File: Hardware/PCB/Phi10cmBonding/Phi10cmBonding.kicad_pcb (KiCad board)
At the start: 4 copper layers, 38.1 x 38.1 mm, 2 parts

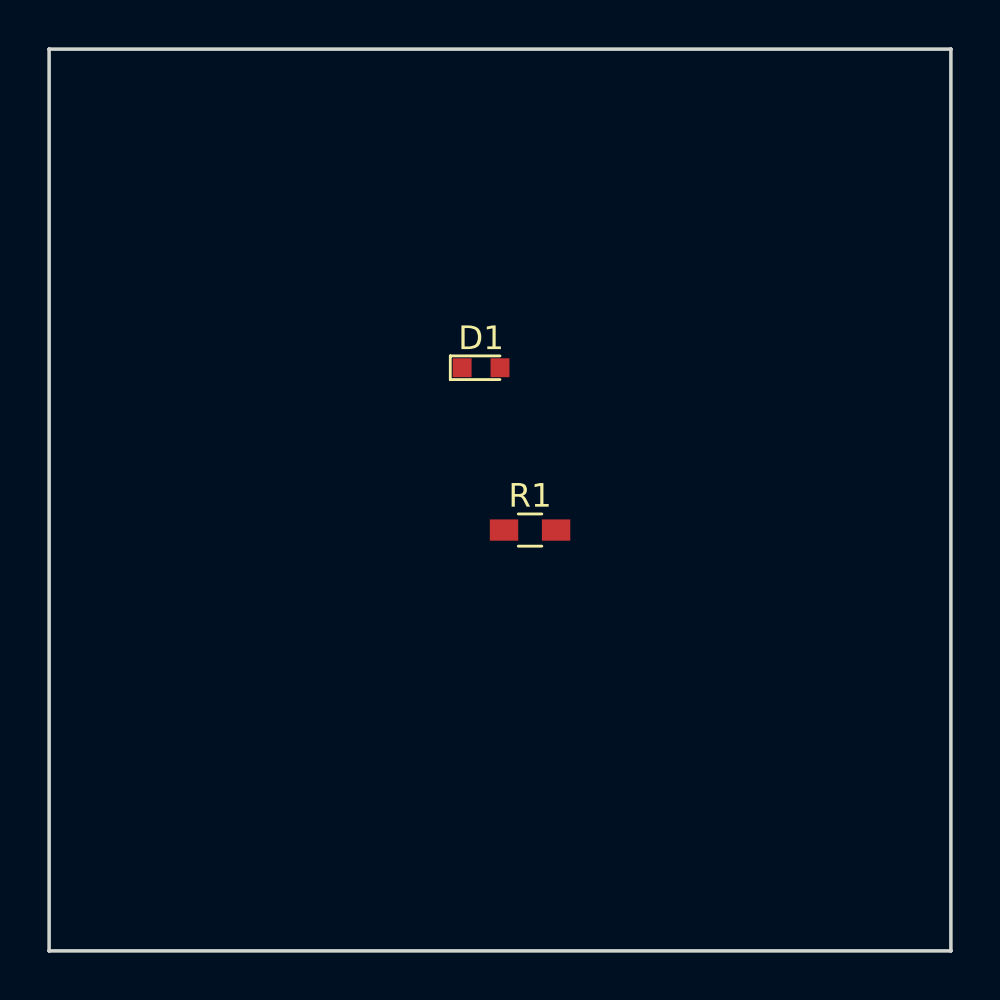
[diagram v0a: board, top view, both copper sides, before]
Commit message: First example of correct net handling and zone filling
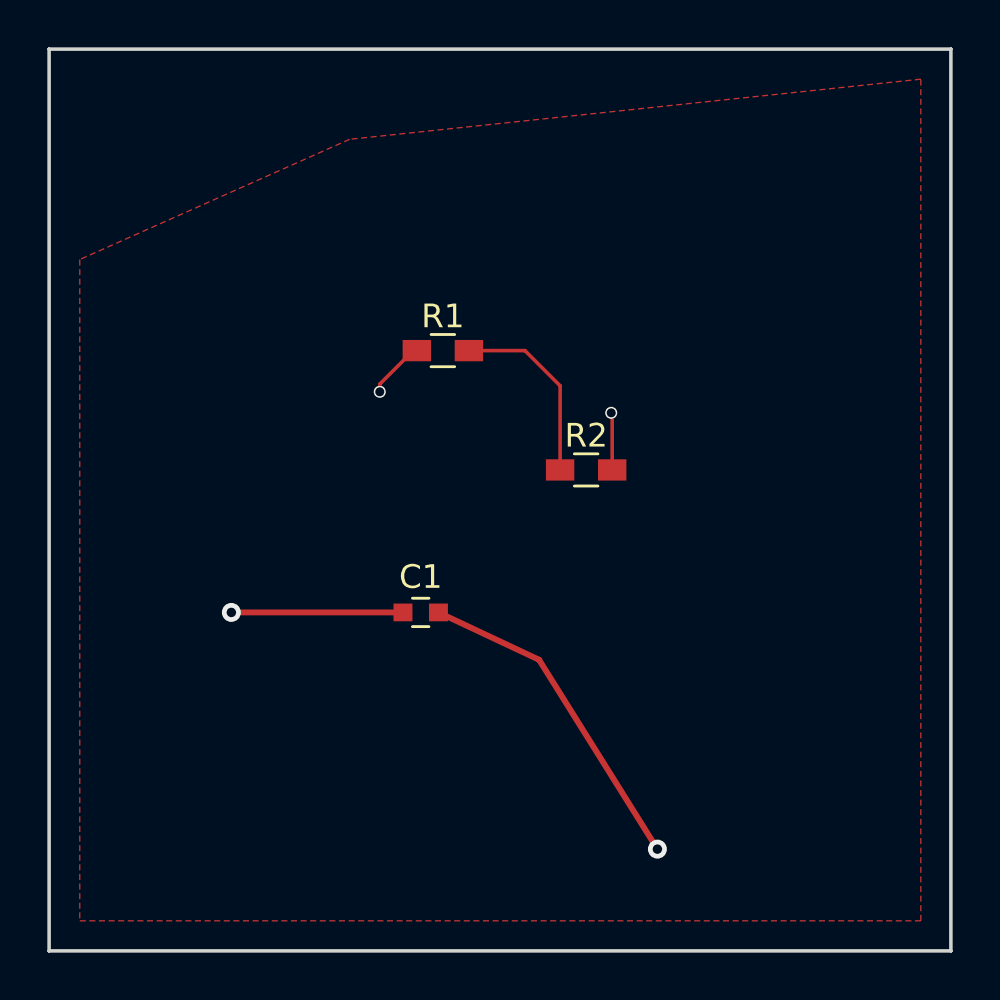
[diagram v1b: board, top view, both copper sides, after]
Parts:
- removed D1: LED, LEDs:LED_0603
- added C1: C_0603, C_0603, F.Cu at (130.0, 100.0)
- added R2: 1k, Resistors_SMD:R_0603_HandSoldering, F.Cu at (137.0, 94.0)
- R1: value R -> 100
- moved R1 8.43 mm to (130.9, 88.9)
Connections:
- R1 pad 1: Net-(D1-Pad2) -> /VDD
- R1 pad 2: (no net) -> /R12
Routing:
- net /GND: track 0.00 -> 16.6 mm, vias 0 -> 2
- net /VDD: track 0.00 -> 9.73 mm, vias 0 -> 2
- net /R12: track 0.00 -> 8.03 mm
- added copper zone on F.Cu, net /GND
- added copper zone on In1.Cu, net /GND
- added copper zone on In2.Cu, net /VDD
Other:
- net class Default: clearance 0.2 -> 0.1016; trace_width 0.25 -> 0.1524; via_dia 0.6 -> 0.508; via_drill 0.4 -> 0.381
- rule trace_clearance: 0.2 -> 0.1016
